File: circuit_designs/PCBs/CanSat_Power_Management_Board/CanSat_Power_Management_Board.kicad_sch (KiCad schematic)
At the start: 50 parts, among them J1 MCU Switch (7.4V), J2 7.4V Battery, J3 Sensor Board, J4 Booster Switch (3.7V), J5 3.7V Battery, Q1 BS170, Q2 BSS84, U1 LM2596T-ADJ, U3 NE555P

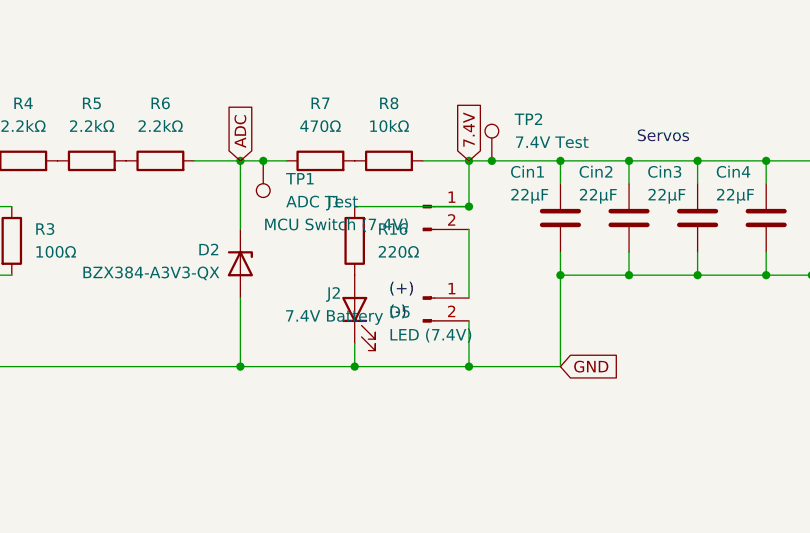
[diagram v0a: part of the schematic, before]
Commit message: fixed errors and exposed copper for thermal pads
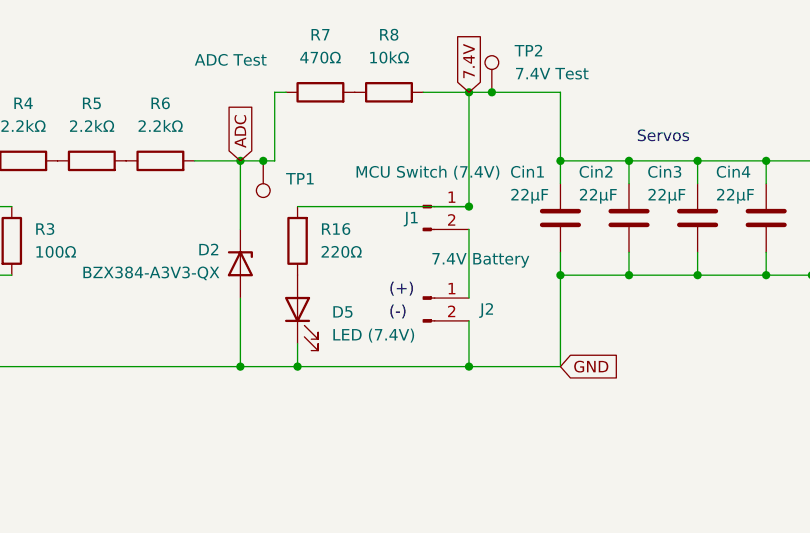
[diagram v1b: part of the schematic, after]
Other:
- moved on the sheet: D5, R16, R7, R8, TP2
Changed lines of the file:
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@@
 	(paper "A4")
 	(junction
-		(at 110.49 44.45)
+		(at 110.49 36.83)
 		(diameter 0)
 		(color 0 0 0 0)
@@
 	)
 	(junction
-		(at 95.25 67.31)
-		(diameter 0)
-		(color 0 0 0 0)
-	)
-	(junction
 		(at 152.4 135.89)
 		(diameter 0)
@@
 	)
 	(junction
+		(at 88.9 67.31)
+		(diameter 0)
+		(color 0 0 0 0)
+	)
+	(junction
 		(at 228.6 119.38)
 		(diameter 0)
@@
 	)
 	(junction
-		(at 107.95 44.45)
+		(at 107.95 36.83)
 		(diameter 0)
 		(color 0 0 0 0)
@@
 	(wire
 		(pts
-			(xy 102.87 44.45) (xy 107.95 44.45)
+			(xy 102.87 36.83) (xy 107.95 36.83)
 		)
 		(stroke
@@
 	(wire
 		(pts
-			(xy 95.25 49.53) (xy 107.95 49.53)
+			(xy 88.9 49.53) (xy 107.95 49.53)
 		)
 		(stroke
@@
 	(wire
 		(pts
-			(xy 107.95 49.53) (xy 107.95 44.45)
+			(xy 107.95 49.53) (xy 107.95 36.83)
 		)
 		(stroke
@@
 	(wire
 		(pts
+			(xy 88.9 67.31) (xy 107.95 67.31)
+		)
+		(stroke
+			(width 0)
+			(type default)
+		)
+	)
+	(wire
+		(pts
 			(xy 36.83 153.67) (xy 39.37 153.67)
 		)
@@
 	(wire
 		(pts
-			(xy 107.95 44.45) (xy 110.49 44.45)
+			(xy 107.95 36.83) (xy 110.49 36.83)
 		)
 		(stroke
@@
 	(wire
 		(pts
+			(xy 86.36 44.45) (xy 85.09 44.45)
+		)
+		(stroke
+			(width 0)
+			(type default)
+		)
+	)
+	(wire
+		(pts
 			(xy 173.99 57.15) (xy 199.39 57.15)
 		)
@@
 	(wire
 		(pts
+			(xy 86.36 36.83) (xy 86.36 44.45)
+		)
+		(stroke
+			(width 0)
+			(type default)
+		)
+	)
+	(wire
+		(pts
 			(xy 140.97 57.15) (xy 146.05 57.15)
 		)
@@
 	(wire
 		(pts
-			(xy 110.49 44.45) (xy 118.11 44.45)
+			(xy 110.49 36.83) (xy 118.11 36.83)
 		)
 		(stroke
@@
 	(wire
 		(pts
-			(xy 95.25 64.77) (xy 95.25 67.31)
+			(xy 88.9 64.77) (xy 88.9 67.31)
 		)
 		(stroke
@@
 	(wire
 		(pts
-			(xy 99.06 143.51) (xy 119.38 143.51)
+			(xy 118.11 36.83) (xy 118.11 44.45)
 		)
 		(stroke
@@
 	(wire
 		(pts
-			(xy 72.39 143.51) (xy 81.28 143.51)
+			(xy 99.06 143.51) (xy 119.38 143.51)
 		)
 		(stroke
@@
 	(wire
 		(pts
-			(xy 201.93 137.16) (xy 215.9 137.16)
+			(xy 72.39 143.51) (xy 81.28 143.51)
 		)
 		(stroke
@@
 	(wire
 		(pts
-			(xy 95.25 67.31) (xy 107.95 67.31)
+			(xy 201.93 137.16) (xy 215.9 137.16)
 		)
 		(stroke
@@
 	(wire
 		(pts
-			(xy 85.09 44.45) (xy 87.63 44.45)
+			(xy 86.36 36.83) (xy 87.63 36.83)
 		)
 		(stroke
@@
 	(wire
 		(pts
-			(xy 82.55 67.31) (xy 95.25 67.31)
+			(xy 82.55 67.31) (xy 88.9 67.31)
 		)
 		(stroke
@@
 	(global_label "7.4V"
 		(shape input)
-		(at 107.95 44.45 90)
+		(at 107.95 36.83 90)
 		(fields_autoplaced yes)
 		(effects
@@
 		)
 		(property "Intersheetrefs" "${INTERSHEET_REFS}"
-			(at 107.95 37.3524 90)
+			(at 107.95 29.7324 90)
 			(effects
 				(font
@@
 		(dnp no)
 		(property "Reference" "J1"
-			(at 92.964 49.022 0)
+			(at 101.6 50.8 0)
 			(effects
 				(font
@@
 		)
 		(property "Value" "MCU Switch (7.4V)"
-			(at 93.218 51.562 0)
+			(at 103.378 45.72 0)
 			(effects
 				(font
@@
 	(symbol
 		(lib_id "Device:LED")
-		(at 95.25 60.96 90)
+		(at 88.9 60.96 90)
 		(unit 1)
 		(exclude_from_sim no)
@@
 		(fields_autoplaced yes)
 		(property "Reference" "D5"
-			(at 99.06 61.2774 90)
+			(at 92.71 61.2774 90)
 			(effects
 				(font
@@
 		)
 		(property "Value" "LED (7.4V)"
-			(at 99.06 63.8174 90)
+			(at 92.71 63.8174 90)
 			(effects
 				(font
@@
 		)
 		(property "Footprint" "DigiKey:WL-SMCW_0603"
-			(at 95.25 60.96 0)
+			(at 88.9 60.96 0)
 			(effects
 				(font
@@
 		)
 		(property "Datasheet" "~"
-			(at 95.25 60.96 0)
+			(at 88.9 60.96 0)
 			(effects
 				(font
@@
 		)
 		(property "Description" "Light emitting diode"
-			(at 95.25 60.96 0)
+			(at 88.9 60.96 0)
 			(effects
 				(font
@@
 	(symbol
 		(lib_id "Device:R")
-		(at 99.06 44.45 90)
+		(at 99.06 36.83 90)
 		(unit 1)
 		(exclude_from_sim no)
@@
 		(fields_autoplaced yes)
 		(property "Reference" "R8"
-			(at 99.06 38.1 90)
+			(at 99.06 30.48 90)
 			(effects
 				(font
@@
 		)
 		(property "Value" "10kΩ"
-			(at 99.06 40.64 90)
+			(at 99.06 33.02 90)
 			(effects
 				(font
@@
 		)
 		(property "Footprint" "Resistor_THT:R_Axial_DIN0207_L6.3mm_D2.5mm_P7.62mm_Horizontal"
-			(at 99.06 46.228 90)
+			(at 99.06 38.608 90)
 			(effects
 				(font
@@
 		)
 		(property "Datasheet" "~"
-			(at 99.06 44.45 0)
+			(at 99.06 36.83 0)
 			(effects
 				(font
@@
 		)
 		(property "Description" "Resistor"
-			(at 99.06 44.45 0)
+			(at 99.06 36.83 0)
 			(effects
 				(font
@@
 		(on_board yes)
 		(dnp no)
-		(fields_autoplaced yes)
 		(property "Reference" "TP1"
 			(at 87.63 46.4819 0)
@@
 		)
 		(property "Value" "ADC Test"
-			(at 87.63 49.0219 0)
+			(at 77.47 33.274 0)
 			(effects
 				(font
@@
 	(symbol
 		(lib_id "Connector:TestPoint")
-		(at 110.49 44.45 0)
+		(at 110.49 36.83 0)
 		(unit 1)
 		(exclude_from_sim no)
@@
 		(fields_autoplaced yes)
 		(property "Reference" "TP2"
-			(at 113.03 39.8779 0)
+			(at 113.03 32.2579 0)
 			(effects
 				(font
@@
 		)
 		(property "Value" "7.4V Test"
-			(at 113.03 42.4179 0)
+			(at 113.03 34.7979 0)
 			(effects
 				(font
@@
 		)
 		(property "Footprint" "TestPoint:TestPoint_THTPad_2.0x2.0mm_Drill1.0mm"
-			(at 115.57 44.45 0)
+			(at 115.57 36.83 0)
 			(effects
 				(font
@@
 		)
 		(property "Datasheet" "~"
-			(at 115.57 44.45 0)
+			(at 115.57 36.83 0)
 			(effects
 				(font
@@
 		)
 		(property "Description" "test point"
-			(at 110.49 44.45 0)
+			(at 110.49 36.83 0)
 			(effects
 				(font
@@
 	(symbol
 		(lib_id "Device:R")
-		(at 95.25 53.34 180)
+		(at 88.9 53.34 180)
 		(unit 1)
 		(exclude_from_sim no)
@@
 		(fields_autoplaced yes)
 		(property "Reference" "R16"
-			(at 97.79 52.0699 0)
+			(at 91.44 52.0699 0)
 			(effects
 				(font
@@
 		)
 		(property "Value" "220Ω"
-			(at 97.79 54.6099 0)
+			(at 91.44 54.6099 0)
 			(effects
 				(font
@@
 		)
 		(property "Footprint" "Resistor_SMD:R_0603_1608Metric_Pad0.98x0.95mm_HandSolder"
-			(at 97.028 53.34 90)
+			(at 90.678 53.34 90)
 			(effects
 				(font
@@
 		)
 		(property "Datasheet" "~"
-			(at 95.25 53.34 0)
+			(at 88.9 53.34 0)
 			(effects
 				(font
@@
 		)
 		(property "Description" "Resistor"
-			(at 95.25 53.34 0)
+			(at 88.9 53.34 0)
 			(effects
 				(font
@@
 		(dnp no)
 		(property "Reference" "J2"
-			(at 92.964 59.182 0)
+			(at 109.982 60.96 0)
 			(effects
 				(font
@@
 		)
 		(property "Value" "7.4V Battery"
-			(at 92.964 61.722 0)
+			(at 109.22 55.372 0)
 			(effects
 				(font
@@
 	(symbol
 		(lib_id "Device:R")
-		(at 91.44 44.45 90)
+		(at 91.44 36.83 90)
 		(unit 1)
 		(exclude_from_sim no)
@@
 		(fields_autoplaced yes)
 		(property "Reference" "R7"
-			(at 91.44 38.1 90)
+			(at 91.44 30.48 90)
 			(effects
 				(font
@@
 		)
 		(property "Value" "470Ω"
-			(at 91.44 40.64 90)
+			(at 91.44 33.02 90)
 			(effects
 				(font
@@
 		)
 		(property "Footprint" "Resistor_THT:R_Axial_DIN0207_L6.3mm_D2.5mm_P7.62mm_Horizontal"
-			(at 91.44 46.228 90)
+			(at 91.44 38.608 90)
 			(effects
 				(font
@@
 		)
 		(property "Datasheet" "~"
-			(at 91.44 44.45 0)
+			(at 91.44 36.83 0)
 			(effects
 				(font
@@
 		)
 		(property "Description" "Resistor"
-			(at 91.44 44.45 0)
+			(at 91.44 36.83 0)
 			(effects
 				(font
